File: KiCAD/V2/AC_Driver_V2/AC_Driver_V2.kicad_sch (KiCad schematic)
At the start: 113 parts, among them J1-120VAC1 Screw_Terminal_01x02, J2 USART6, J2-HVDC2 Screw_Terminal_01x02, J3 USB_B_Micro, J4 Conn_01x05_Pin, J5 USART2, J6 Receiver, Q1 2N3904, SW1 SW_Push, SW2 SW_SPDT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

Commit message: V2 tested and working - WIP
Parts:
- added C5: 4u7, Capacitor_SMD:C_0805_2012Metric, symbol Device:C
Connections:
- net +3.3V: now also R1.1; no longer R1.2
- net GND: now also C38.1, C39.1, C40.1, SW1.1, C5.2
- net NRST: now also R1.2
- net at D1.2 (A): now also C38.2, R23.2; no longer C38.1
- net at D2.2 (A): now also C39.2, R24.2; no longer C39.1
- net at D3.2 (A): now also C40.2, R25.2; no longer C40.1
- net at U4.30 (VCAP1): now also C5.1
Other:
- moved on the sheet: C38, C39, C40, D1, D2, D3, R1, R24, R25

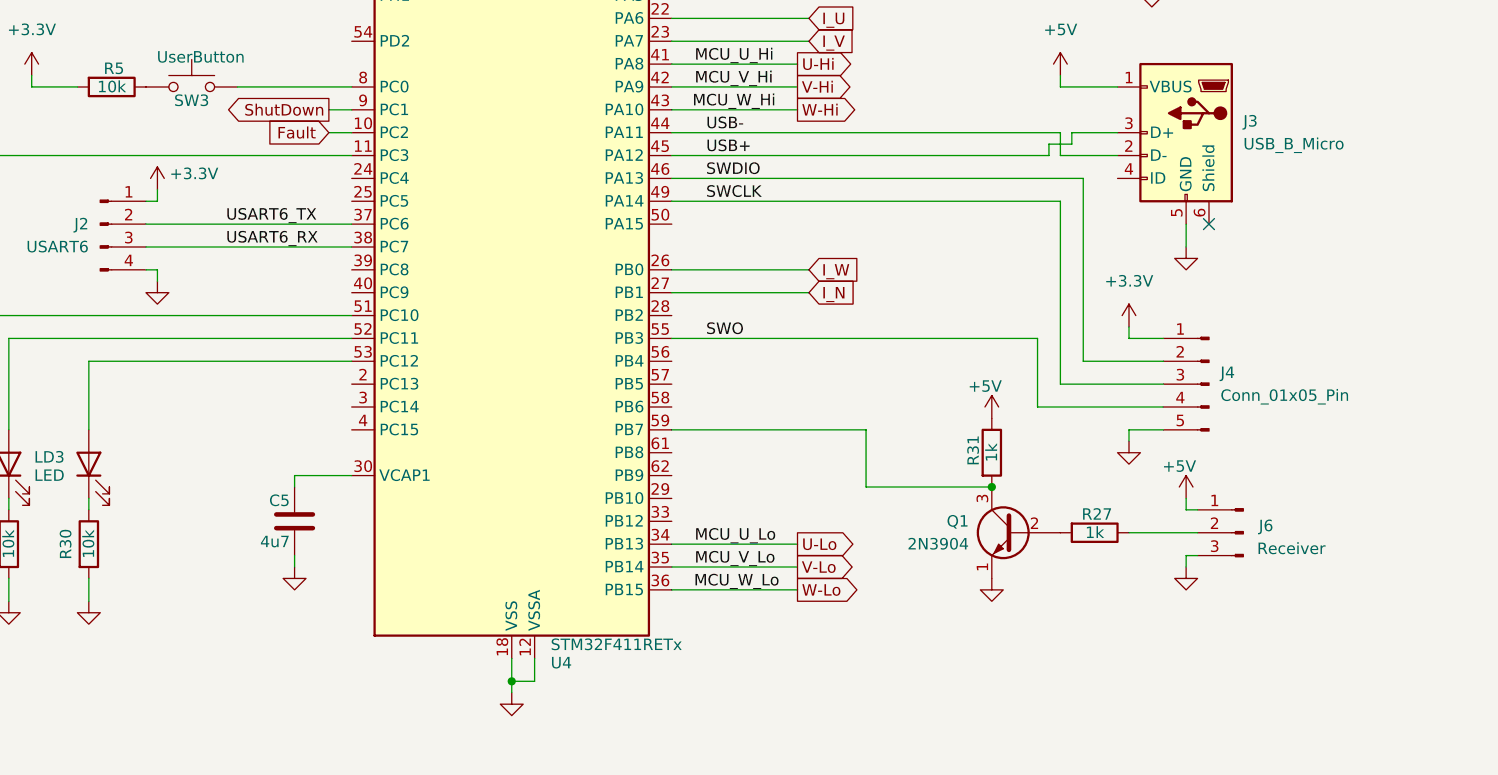
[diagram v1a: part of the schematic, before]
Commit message: corrects receiver pins
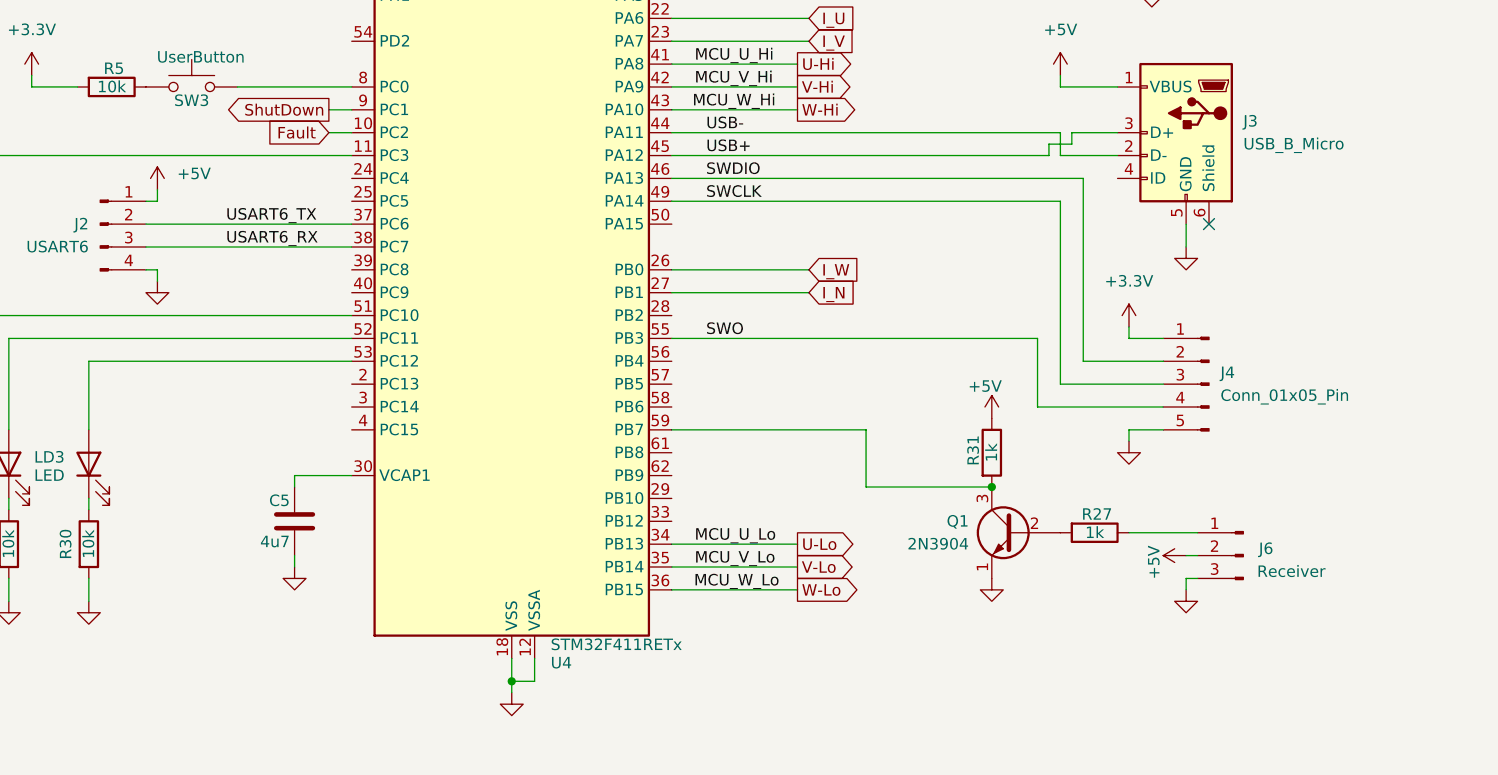
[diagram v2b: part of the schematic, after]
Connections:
- net +3.3V: no longer J2.1 (Pin_1)
- net +5V: now also J2.1 (Pin_1), J6.2 (Pin_2); no longer J6.1 (Pin_1)
- net at R27.1: now also J6.1 (Pin_1); no longer J6.2 (Pin_2)
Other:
- moved on the sheet: J6
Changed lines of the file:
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@@
 	(wire
 		(pts
+			(xy 229.87 257.81) (xy 231.14 257.81)
+		)
+		(stroke
+			(width 0)
+			(type default)
+		)
+	)
+	(wire
+		(pts
 			(xy 190.5 29.21) (xy 200.66 29.21)
 		)
@@
 	(wire
 		(pts
-			(xy 231.14 252.73) (xy 229.87 252.73)
-		)
-		(stroke
-			(width 0)
-			(type default)
-		)
-	)
-	(wire
-		(pts
 			(xy 365.76 114.3) (xy 365.76 111.76)
 		)
@@
 	(wire
 		(pts
-			(xy 223.52 255.27) (xy 231.14 255.27)
-		)
-		(stroke
-			(width 0)
-			(type default)
-		)
-	)
-	(wire
-		(pts
 			(xy 195.58 80.01) (xy 200.66 80.01)
 		)
@@
 	(wire
 		(pts
-			(xy 231.14 257.81) (xy 229.87 257.81)
+			(xy 231.14 260.35) (xy 229.87 260.35)
 		)
 		(stroke
@@
 	(wire
 		(pts
-			(xy 229.87 252.73) (xy 229.87 251.46)
-		)
-		(stroke
-			(width 0)
-			(type default)
-		)
-	)
-	(wire
-		(pts
 			(xy 195.58 121.92) (xy 219.71 121.92)
 		)
@@
 	(wire
 		(pts
+			(xy 231.14 255.27) (xy 223.52 255.27)
+		)
+		(stroke
+			(width 0)
+			(type default)
+		)
+	)
+	(wire
+		(pts
 			(xy 133.35 165.1) (xy 139.7 165.1)
 		)
@@
 	(wire
 		(pts
-			(xy 229.87 257.81) (xy 229.87 259.08)
+			(xy 229.87 260.35) (xy 229.87 261.62)
 		)
 		(stroke
@@
 	(symbol
 		(lib_id "Connector:Conn_01x03_Pin")
-		(at 236.22 255.27 0)
+		(at 236.22 257.81 0)
 		(mirror y)
 		(unit 1)
@@
 		(dnp no)
 		(property "Reference" "J6"
-			(at 238.76 254.508 0)
+			(at 238.76 257.048 0)
 			(effects
 				(font
@@
 		)
 		(property "Value" "Receiver"
-			(at 241.554 257.048 0)
+			(at 241.554 259.588 0)
 			(effects
 				(font
@@
 		)
 		(property "Footprint" "Connector_PinHeader_2.54mm:PinHeader_1x03_P2.54mm_Vertical"
-			(at 236.22 255.27 0)
+			(at 236.22 257.81 0)
 			(effects
 				(font
@@
 		)
 		(property "Datasheet" "~"
-			(at 236.22 255.27 0)
+			(at 236.22 257.81 0)
 			(effects
 				(font
@@
 		)
 		(property "Description" "Generic connector, single row, 01x03, script generated"
-			(at 236.22 255.27 0)
+			(at 236.22 257.81 0)
 			(effects
 				(font
@@
 			)
 		)
-		(property "Value" "+3.3V"
+		(property "Value" "+5V"
 			(at 119.634 215.392 0)
 			(effects
@@
 	(symbol
 		(lib_id "power:+5V")
-		(at 229.87 251.46 0)
+		(at 229.87 257.81 90)
 		(unit 1)
 		(exclude_from_sim no)
@@
 		(dnp no)
 		(property "Reference" "#PWR070"
-			(at 229.87 255.27 0)
+			(at 233.68 257.81 0)
 			(effects
 				(font
@@
 		)
 		(property "Value" "+5V"
-			(at 229.108 247.904 0)
+			(at 226.314 258.572 0)
 			(effects
 				(font
@@
 		)
 		(property "Footprint" ""
-			(at 229.87 251.46 0)
+			(at 229.87 257.81 0)
 			(effects
 				(font
@@
 		)
 		(property "Datasheet" ""
-			(at 229.87 251.46 0)
+			(at 229.87 257.81 0)
 			(effects
 				(font
@@
 		)
 		(property "Description" "Power symbol creates a global label with name \"+5V\""
-			(at 229.87 251.46 0)
+			(at 229.87 257.81 0)
 			(effects
 				(font
@@
 	(symbol
 		(lib_id "power:GND")
-		(at 229.87 259.08 0)
+		(at 229.87 261.62 0)
 		(unit 1)
 		(exclude_from_sim no)
@@
 		(fields_autoplaced yes)
 		(property "Reference" "#PWR071"
-			(at 229.87 265.43 0)
+			(at 229.87 267.97 0)
 			(effects
 				(font
@@
 		)
 		(property "Value" "GND"
-			(at 229.87 264.16 0)
+			(at 229.87 266.7 0)
 			(effects
 				(font
@@
 		)
 		(property "Footprint" ""
-			(at 229.87 259.08 0)
+			(at 229.87 261.62 0)
 			(effects
 				(font
@@
 		)
 		(property "Datasheet" ""
-			(at 229.87 259.08 0)
+			(at 229.87 261.62 0)
 			(effects
 				(font
@@
 		)
 		(property "Description" ""
-			(at 229.87 259.08 0)
+			(at 229.87 261.62 0)
 			(effects
 				(font

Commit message: sync
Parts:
- removed C3: 10p, Capacitor_SMD:C_0805_2012Metric, symbol Device:C
- C4: value 10p -> 10n
- J2: value USART6 -> Encoder
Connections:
- net GND: no longer C4.2
- net HSE_IN: now also C4.1
- net HSE_OUT: now also C4.2; no longer C4.1
- net USART6_RX renamed ChB
- net USART6_TX renamed ChA
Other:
- moved on the sheet: C4, Y1

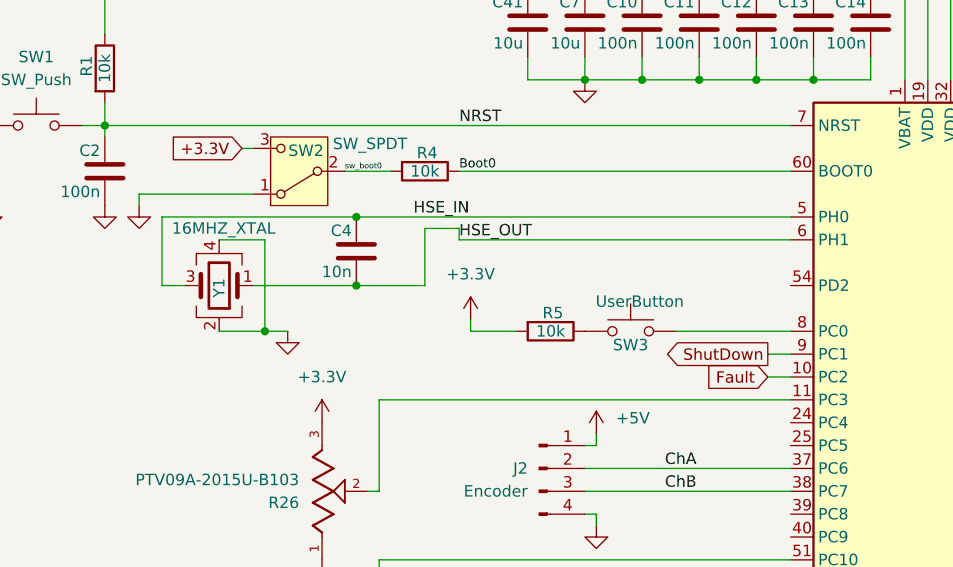
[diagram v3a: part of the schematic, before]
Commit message: adds potentiameter to control the speed
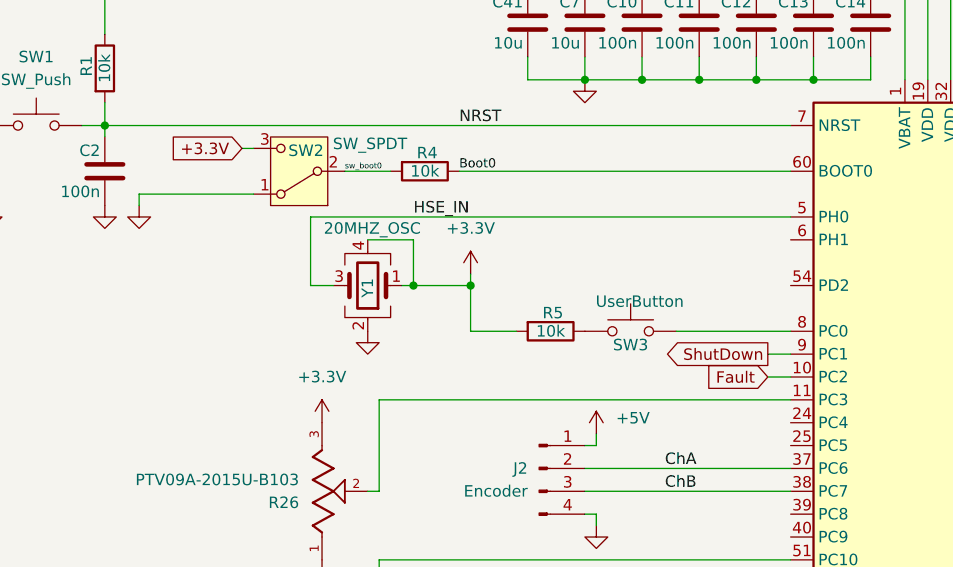
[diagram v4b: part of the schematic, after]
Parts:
- removed C4: 10n, Capacitor_SMD:C_0805_2012Metric, symbol Device:C
- Y1: value 16MHZ_XTAL -> 20MHZ_OSC
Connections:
- net +3.3V: now also Y1.1, Y1.4
- net GND: no longer Y1.4
- net HSE_OUT: no longer names the net of U4.6 (PH1)
- net HSE_OUT: no longer Y1.1
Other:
- moved on the sheet: Y1
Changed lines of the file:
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@@
 	)
 	(junction
-		(at 127 165.1)
+		(at 101.6 200.66)
 		(diameter 0)
 		(color 0 0 0 0)
 	)
 	(junction
-		(at 88.9 193.04)
+		(at 127 165.1)
 		(diameter 0)
 		(color 0 0 0 0)
@@
 	)
 	(junction
-		(at 78.74 205.74)
-		(diameter 0)
-		(color 0 0 0 0)
-	)
-	(junction
-		(at 88.9 200.66)
-		(diameter 0)
-		(color 0 0 0 0)
-	)
-	(junction
 		(at 359.41 124.46)
 		(diameter 0)
@@
 	)
 	(junction
+		(at 95.25 200.66)
+		(diameter 0)
+		(color 0 0 0 0)
+	)
+	(junction
 		(at 114.3 165.1)
 		(diameter 0)
@@
 	(wire
 		(pts
+			(xy 95.25 195.58) (xy 95.25 200.66)
+		)
+		(stroke
+			(width 0)
+			(type default)
+		)
+	)
+	(wire
+		(pts
 			(xy 215.9 213.36) (xy 222.25 213.36)
 		)
@@
 	(wire
 		(pts
-			(xy 88.9 193.04) (xy 137.16 193.04)
+			(xy 83.82 193.04) (xy 137.16 193.04)
 		)
 		(stroke
@@
 	(wire
 		(pts
-			(xy 100.33 195.58) (xy 137.16 195.58)
-		)
-		(stroke
-			(width 0)
-			(type default)
-		)
-	)
-	(wire
-		(pts
 			(xy 243.84 107.95) (xy 243.84 110.49)
 		)
@@
 	(wire
 		(pts
-			(xy 101.6 204.47) (xy 101.6 205.74)
+			(xy 101.6 199.39) (xy 101.6 200.66)
 		)
 		(stroke
@@
 	(wire
 		(pts
-			(xy 73.66 205.74) (xy 78.74 205.74)
-		)
-		(stroke
-			(width 0)
-			(type default)
-		)
-	)
-	(wire
-		(pts
 			(xy 223.52 233.68) (xy 223.52 232.41)
 		)
@@
 	(wire
 		(pts
-			(xy 96.52 194.31) (xy 100.33 194.31)
-		)
-		(stroke
-			(width 0)
-			(type default)
-		)
-	)
-	(wire
-		(pts
 			(xy 339.09 140.97) (xy 339.09 111.76)
 		)
@@
 	(wire
 		(pts
-			(xy 88.9 200.66) (xy 77.47 200.66)
+			(xy 93.98 200.66) (xy 95.25 200.66)
 		)
 		(stroke
@@
 	(wire
 		(pts
-			(xy 100.33 194.31) (xy 100.33 195.58)
-		)
-		(stroke
-			(width 0)
-			(type default)
-		)
-	)
-	(wire
-		(pts
 			(xy 172.72 203.2) (xy 186.69 203.2)
 		)
@@
 	(wire
 		(pts
-			(xy 73.66 195.58) (xy 78.74 195.58)
+			(xy 90.17 195.58) (xy 95.25 195.58)
 		)
 		(stroke
@@
 	(wire
 		(pts
-			(xy 78.74 205.74) (xy 81.28 205.74)
+			(xy 95.25 200.66) (xy 101.6 200.66)
 		)
 		(stroke
@@
 	(wire
 		(pts
-			(xy 67.31 193.04) (xy 88.9 193.04)
-		)
-		(stroke
-			(width 0)
-			(type default)
-		)
-	)
-	(wire
-		(pts
 			(xy 288.29 113.03) (xy 288.29 116.84)
 		)
@@
 	(wire
 		(pts
+			(xy 101.6 200.66) (xy 101.6 205.74)
+		)
+		(stroke
+			(width 0)
+			(type default)
+		)
+	)
+	(wire
+		(pts
 			(xy 231.14 260.35) (xy 229.87 260.35)
 		)
@@
 	(wire
 		(pts
-			(xy 67.31 193.04) (xy 67.31 200.66)
+			(xy 83.82 193.04) (xy 83.82 200.66)
 		)
 		(stroke
@@
 	(wire
 		(pts
-			(xy 67.31 200.66) (xy 69.85 200.66)
+			(xy 83.82 200.66) (xy 86.36 200.66)
 		)
 		(stroke
@@
 	(wire
 		(pts
-			(xy 96.52 194.31) (xy 96.52 200.66)
-		)
-		(stroke
-			(width 0)
-			(type default)
-		)
-	)
-	(wire
-		(pts
 			(xy 304.8 83.82) (xy 238.76 83.82)
 		)
@@
 	(wire
 		(pts
-			(xy 96.52 200.66) (xy 88.9 200.66)
-		)
-		(stroke
-			(width 0)
-			(type default)
-		)
-	)
-	(wire
-		(pts
 			(xy 154.94 177.8) (xy 154.94 165.1)
 		)
@@
 	(wire
 		(pts
-			(xy 78.74 195.58) (xy 78.74 205.74)
-		)
-		(stroke
-			(width 0)
-			(type default)
-		)
-	)
-	(wire
-		(pts
 			(xy 229.87 142.24) (xy 290.83 142.24)
 		)
@@
 		)
 	)
-	(label "HSE_OUT"
-		(at 100.33 195.58 0)
-		(fields_autoplaced yes)
-		(effects
-			(font
-				(size 1.27 1.27)
-			)
-			(justify left bottom)
-		)
-	)
 	(label "U_Lo"
 		(at 293.37 91.44 0)
@@
 	(symbol
 		(lib_id "power:+3.3V")
-		(at 101.6 204.47 0)
+		(at 101.6 199.39 0)
 		(unit 1)
 		(exclude_from_sim no)
@@
 		(fields_autoplaced yes)
 		(property "Reference" "#PWR015"
-			(at 101.6 208.28 0)
+			(at 101.6 203.2 0)
 			(effects
 				(font
@@
 		)
 		(property "Value" "+3.3V"
-			(at 101.6 199.39 0)
+			(at 101.6 194.31 0)
 			(effects
 				(font
@@
 		)
 		(property "Footprint" ""
-			(at 101.6 204.47 0)
+			(at 101.6 199.39 0)
 			(effects
 				(font
@@
 		)
 		(property "Datasheet" ""
-			(at 101.6 204.47 0)
+			(at 101.6 199.39 0)
 			(effects
 				(font
@@
 		)
 		(property "Description" "Power symbol creates a global label with name \"+3.3V\""
-			(at 101.6 204.47 0)
+			(at 101.6 199.39 0)
 			(effects
 				(font
@@
 	(symbol
 		(lib_id "power:GND")
-		(at 81.28 205.74 0)
+		(at 90.17 205.74 0)
 		(unit 1)
 		(exclude_from_sim no)
@@
 		(fields_autoplaced yes)
 		(property "Reference" "#PWR010"
-			(at 81.28 212.09 0)
+			(at 90.17 212.09 0)
 			(effects
 				(font
@@
 		)
 		(property "Value" "GND"
-			(at 81.28 210.82 0)
+			(at 90.17 210.82 0)
 			(effects
 				(font
@@
 		)
 		(property "Footprint" ""
-			(at 81.28 205.74 0)
+			(at 90.17 205.74 0)
 			(effects
 				(font
@@
 		)
 		(property "Datasheet" ""
-			(at 81.28 205.74 0)
+			(at 90.17 205.74 0)
 			(effects
 				(font
@@
 		)
 		(property "Description" ""
-			(at 81.28 205.74 0)
+			(at 90.17 205.74 0)
 			(effects
 				(font
@@
 	(symbol
 		(lib_id "Device:Crystal_GND24")
-		(at 73.66 200.66 180)
+		(at 90.17 200.66 180)
 		(unit 1)
 		(exclude_from_sim no)
@@
 		(dnp no)
 		(property "Reference" "Y1"
-			(at 73.66 200.914 90)
+			(at 90.17 200.914 90)
 			(effects
 				(font
@@
 			)
 		)
-		(property "Value" "16MHZ_XTAL"
-			(at 74.168 194.31 0)
+		(property "Value" "20MHZ_OSC"
+			(at 90.678 194.31 0)
 			(effects
 				(font
@@
 		)
 		(property "Footprint" "Crystal:Crystal_SMD_Abracon_ABM3C-4Pin_5.0x3.2mm"
-			(at 73.66 200.66 0)
+			(at 90.17 200.66 0)
 			(effects
 				(font
@@
 		)
 		(property "Datasheet" "~"
-			(at 73.66 200.66 0)
+			(at 90.17 200.66 0)
 			(effects
 				(font
@@
 		)
 		(property "Description" "Four pin crystal, GND on pins 2 and 4"
-			(at 73.66 200.66 0)
+			(at 90.17 200.66 0)
 			(effects
 				(font
@@
 					(unit 1)
 				)
-			)
-		)
-	)
-	(symbol
-		(lib_id "Device:C")
-		(at 88.9 196.85 0)
-		(mirror y)
-		(unit 1)
-		(exclude_from_sim no)
-		(in_bom yes)
-		(on_board yes)
-		(dnp no)
-		(property "Reference" "C4"
-			(at 88.392 194.564 0)
-			(effects
-				(font
-					(size 1.27 1.27)
-				)
-				(justify left)
-			)
-		)
-		(property "Value" "10n"
-			(at 88.392 199.136 0)
-			(effects
-				(font
-					(size 1.27 1.27)
-				)
-				(justify left)
-			)
-		)
-		(property "Footprint" "Capacitor_SMD:C_0805_2012Metric"
-			(at 87.9348 200.66 0)
-			(effects
-				(font
-					(size 1.27 1.27)
-				)
-				(hide yes)
-			)
-		)
-		(property "Datasheet" "~"
-			(at 88.9 196.85 0)
-			(effects
-				(font
-					(size 1.27 1.27)
-				)
-				(hide yes)
-			)
-		)
-		(property "Description" ""
-			(at 88.9 196.85 0)
-			(effects
-				(font
-					(size 1.27 1.27)
-				)
-				(hide yes)
-			)
-		)
-		(pin "1"
-		)
-		(pin "2"
-		)
-		(instances
-			(project "AC_Driver_V2"
-				(path "/6c84e7e9-5412-41af-a048-5fdcbfc30a10"
-					(reference "C4")
-					(unit 1)
-				)
